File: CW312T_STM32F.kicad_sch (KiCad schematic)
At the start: 25 parts, among them J1 HDR_6_2.54, P1 PCIEx4 EDGE CONNECTOR, U1 STM32F100RBT6B

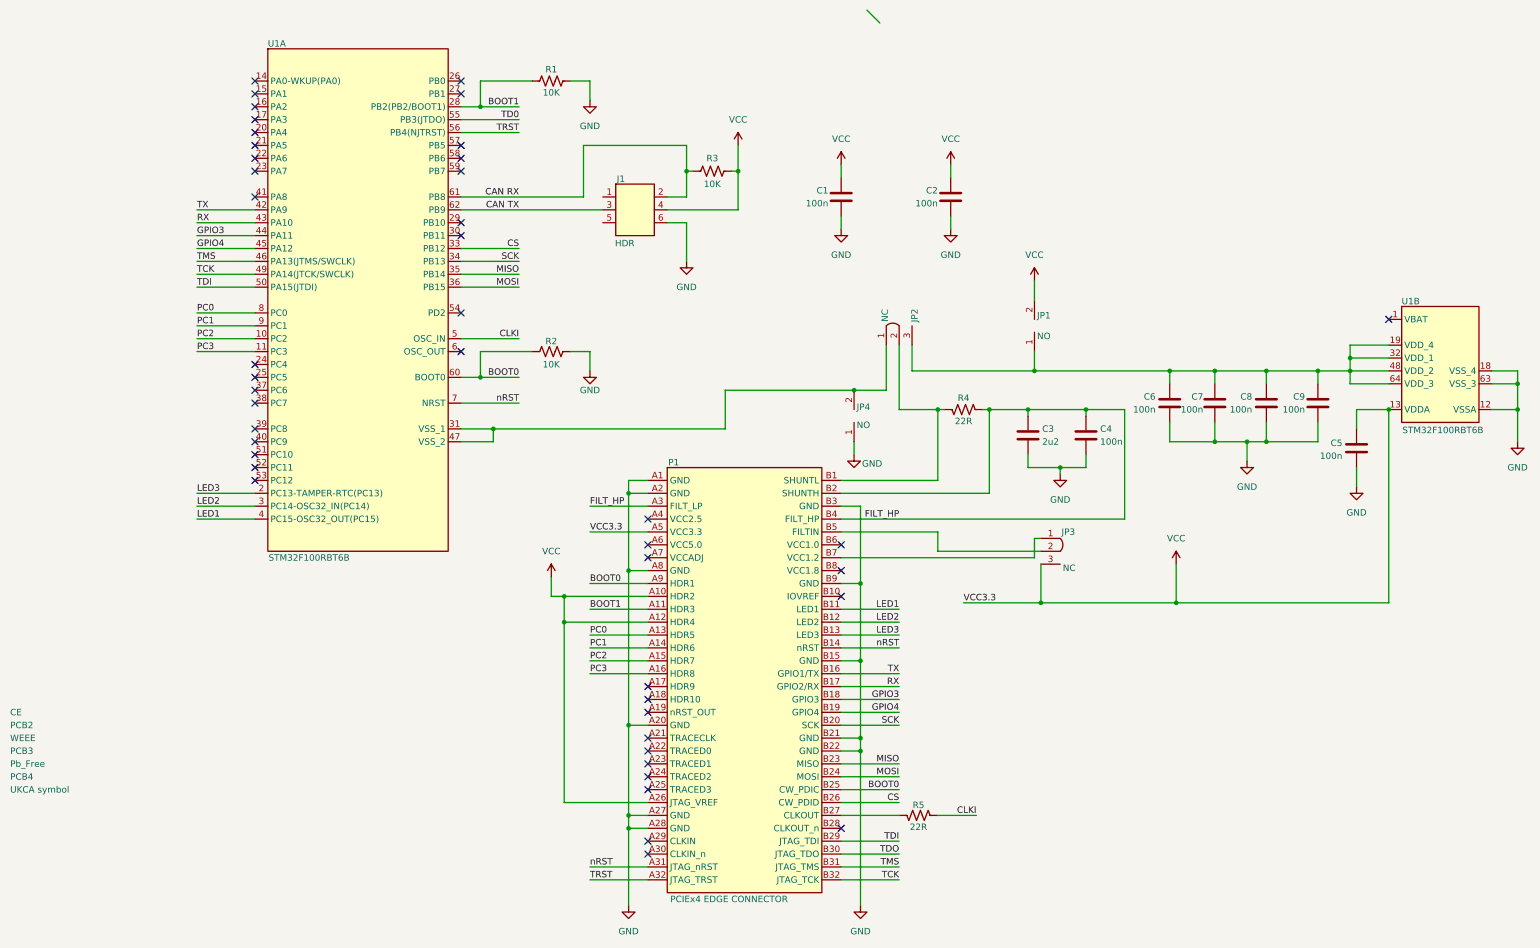
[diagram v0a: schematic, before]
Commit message: updated schematic and pcb after library reorganization, and updated pin header to include proper footprint
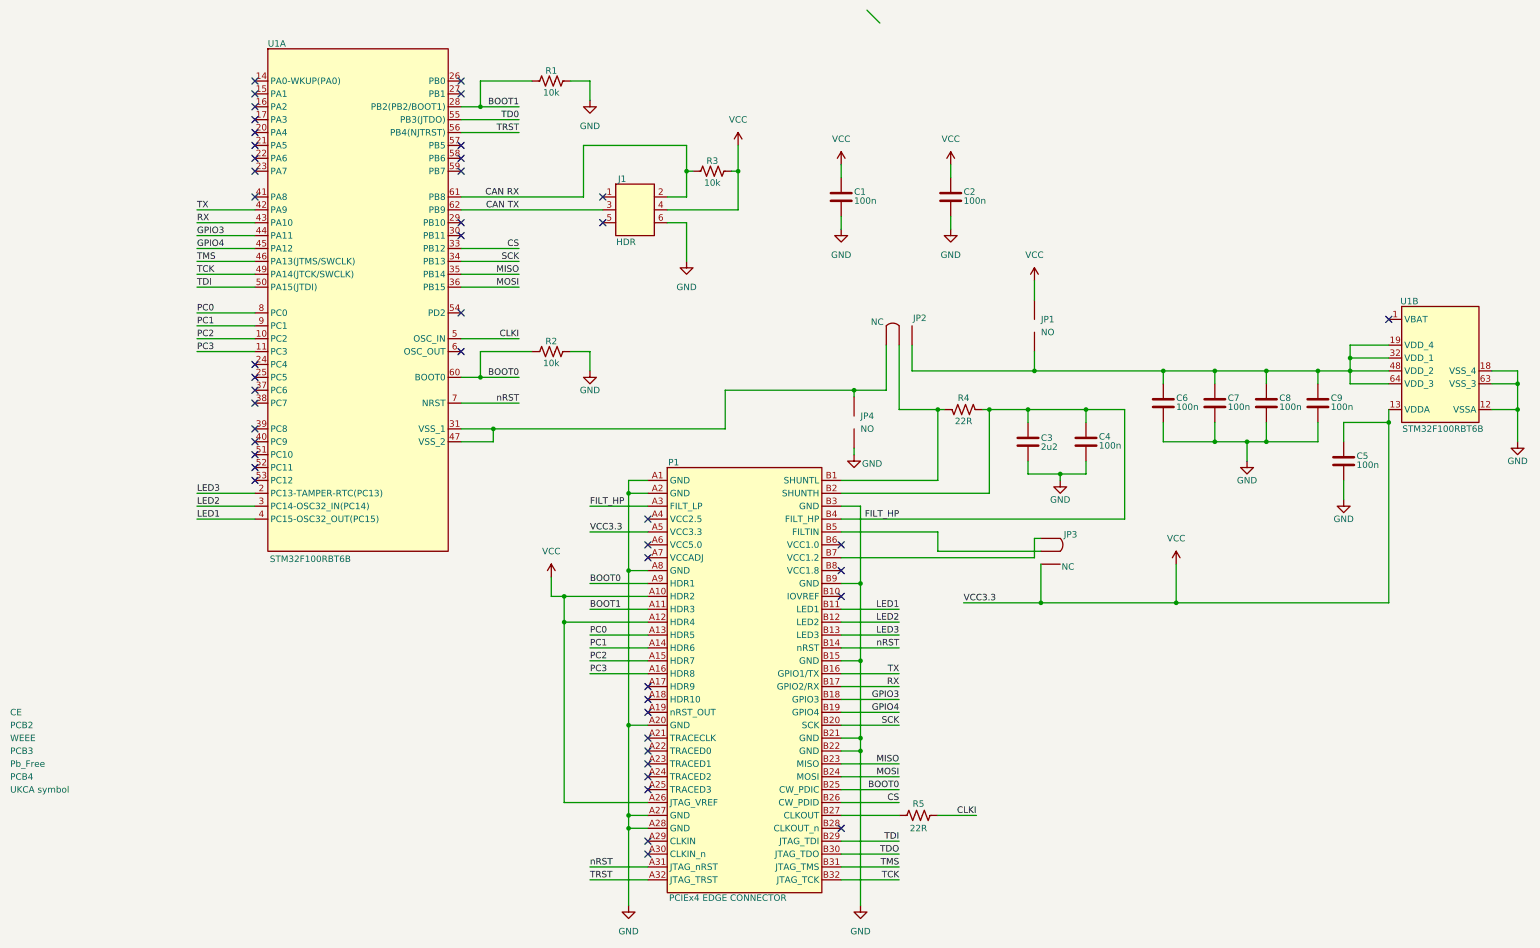
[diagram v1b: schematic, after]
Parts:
- removed C1, C2, C4, C5, C6, C7, C8, C9: CAP_100n_50V_0603, Capacitor_SMD:C_0603_1608Metric, symbol tutorial_2_library:CAP_100n_50V_0603
- removed C3: CAP_2u2_16V_0603, Capacitor_SMD:C_0603_1608Metric, symbol tutorial_2_library:CAP_2u2_16V_0603
- removed J1: HDR_6_2.54, Connector_PinHeader_1.00mm:PinHeader_2x03_P1.00mm_Vertical, symbol tutorial_2_library:VERT_HDR_6_2.54mm
- removed JP1, JP4: ~, Jumper:SolderJumper-2_P1.3mm_Open_Pad1.0x1.5mm, symbol tutorial_2_library:Solder_Jumper_2_NO
- removed JP2, JP3: ~, Jumper:SolderJumper-3_P1.3mm_Bridged2Bar12_Pad1.0x1.5mm, symbol tutorial_2_library:Solder_Jumper_3_NC_1
- removed P1: PCIEx4 EDGE CONNECTOR, tutorial_2_library:CW312_Template, symbol tutorial_2_library:CW312T-Template
- removed R1, R2, R3: 10K, Resistor_SMD:R_0603_1608Metric, symbol tutorial_2_library:RES_10K_0603
- removed R5: 51R_0603, Resistor_SMD:R_0603_1608Metric, symbol tutorial_2_library:RES_51R_0603
- removed U1: STM32F100RBT6B, Package_QFP:TQFP-64_10x10mm_P0.5mm, symbol tutorial_2_library:STM32F100RBT6B
- added C1, C2, C4, C5, C6, C7, C8, C9: CAP_100n_25V_0603, Capacitor_SMD:C_0603_1608Metric, symbol nae_caps:CAP_100n_25V_0603
- added C3: CAP_2u2_10V_0603, Capacitor_SMD:C_0603_1608Metric, symbol nae_caps:CAP_2u2_10V_0603
- added J1: HDR_2x3_2.54, Connector_PinHeader_2.54mm:PinHeader_2x03_P2.54mm_Vertical, symbol NAE_Connectors:VERT_HDR_2x3_2.54mm
- added JP1, JP4: ~, Jumper:SolderJumper-2_P1.3mm_Open_Pad1.0x1.5mm, symbol NAE_Connectors:Solder_Jumper_2_NO
- added JP2, JP3: ~, Jumper:SolderJumper-3_P1.3mm_Bridged2Bar12_Pad1.0x1.5mm, symbol NAE_Connectors:Solder_Jumper_3_NC_1
- added P1: PCIEx4 EDGE CONNECTOR, tutorial_2_library:CW312_Template, symbol NAE_Connectors:CW312T-Template
- added R1, R2, R3: RES_10k_0603, Resistor_SMD:R_0603_1608Metric, symbol 0603_Yageo_Res:RES_10k_0603
- added R5: RES_22R_0603, Resistor_SMD:R_0603_1608Metric, symbol 0603_Yageo_Res:RES_22R_0603
- added U1: STM32F100RBT6B, Package_QFP:TQFP-64_10x10mm_P0.5mm, symbol NAE_Integrated_Circuits:STM32F100RBT6B
- PCB4: now left out of the parts list
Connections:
- net BOOT0: now also P1.A9 (HDR1), P1.B25 (CW_PDIC), R2.1, U1.60 (BOOT0)
- net BOOT1: now also P1.A11 (HDR3), R1.1, U1.28 (PB2(PB2/BOOT1))
- net CAN RX: now also J1.2, R3.1, U1.61 (PB8)
- net CAN TX: now also J1.3, U1.62 (PB9)
- net CLKI: now also R5.2, U1.5 (OSC_IN)
- net CS: now also P1.B26 (CW_PDID), U1.33 (PB12)
- net FILT_HP: now also C3.2, C4.2, P1.A3 (FILT_LP), P1.B2 (SHUNTH), P1.B4 (FILT_HP)
- net GND: now also C1.1, C2.1, C3.1, C4.1, C5.1, C6.1, C7.1, C8.1, C9.1, J1.6, JP4.1, P1.A1 (GND), P1.A2 (GND), P1.A20 (GND), P1.A27 (GND), P1.A28 (GND), P1.A8 (GND), P1.B15 (GND), P1.B21 (GND), P1.B22 (GND), P1.B3 (GND), P1.B9 (GND), R1.2, R2.2, U1.12 (VSSA), U1.18 (VSS_4), U1.63 (VSS_3)
- net GPIO3: now also P1.B18 (GPIO3), U1.44 (PA11)
- net GPIO4: now also P1.B19 (GPIO4), U1.45 (PA12)
- net LED1: now also P1.B11 (LED1), U1.4 (PC15-OSC32_OUT(PC15))
- net LED2: now also P1.B12 (LED2), U1.3 (PC14-OSC32_IN(PC14))
- net LED3: now also P1.B13 (LED3), U1.2 (PC13-TAMPER-RTC(PC13))
- net MISO: now also P1.B23 (MISO), U1.35 (PB14)
- net MOSI: now also P1.B24 (MOSI), U1.36 (PB15)
- net PC0: now also P1.A13 (HDR5), U1.8 (PC0)
- net PC1: now also P1.A14 (HDR6), U1.9 (PC1)
- net PC2: now also P1.A15 (HDR7), U1.10 (PC2)
- net PC3: now also P1.A16 (HDR8), U1.11 (PC3)
- net RX: now also P1.B17 (GPIO2/RX), U1.43 (PA10)
- net SCK: now also P1.B20 (SCK), U1.34 (PB13)
- net TCK: now also P1.B32 (JTAG_TCK), U1.49 (PA14(JTCK/SWCLK))
- net TD0: now also U1.55 (PB3(JTDO))
- net TDI: now also P1.B29 (JTAG_TDI), U1.50 (PA15(JTDI))
- net TDO: now also P1.B30 (JTAG_TDO)
- net TMS: now also P1.B31 (JTAG_TMS), U1.46 (PA13(JTMS/SWCLK))
- net TRST: now also P1.A32 (JTAG_TRST), U1.56 (PB4(NJTRST))
- net TX: now also P1.B16 (GPIO1/TX), U1.42 (PA9)
- net VCC: now also C1.2, C2.2, C5.2, J1.4, JP1.2, JP3.3, P1.A10 (HDR2), P1.A12 (HDR4), P1.A26 (JTAG_VREF), P1.A5 (VCC3.3), R3.2, U1.13 (VDDA)
- net nRST: now also P1.A31 (JTAG_nRST), P1.B14 (nRST), U1.7 (NRST)
- net at R4.1: now also JP2.2, P1.B1 (SHUNTL)
- new net: JP2.1, JP4.2, U1.31 (VSS_1), U1.47 (VSS_2)
- new net: C6.2, C7.2, C8.2, C9.2, JP1.1, JP2.3, U1.19 (VDD_4), U1.32 (VDD_1), U1.48 (VDD_2), U1.64 (VDD_3)
- new net: P1.B27 (CLKOUT), R5.1
- new net: JP3.2, P1.B5 (FILTIN)
- new net: JP3.1, P1.B7 (VCC1.2)
- no-connect marks 45 -> 47
